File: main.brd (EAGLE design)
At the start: 45.1 x 39.4 mm, 12 parts, among them IC1 4001N, IC2 4069N, IC3 ISO1050DUB, IC4 ISO1050DUB, IC5 LD117AV33

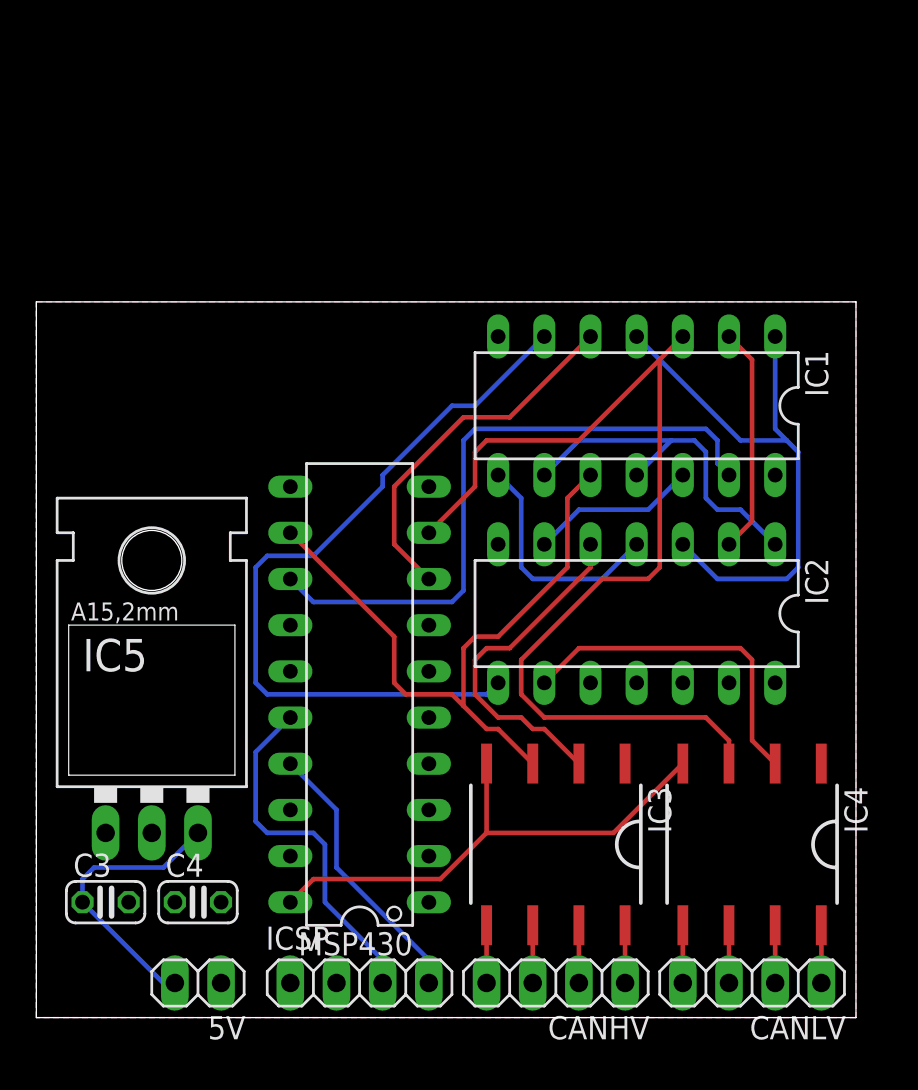
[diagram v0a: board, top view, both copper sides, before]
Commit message: Pin pitch of TI's MSP430 N20 package now aligns with grid
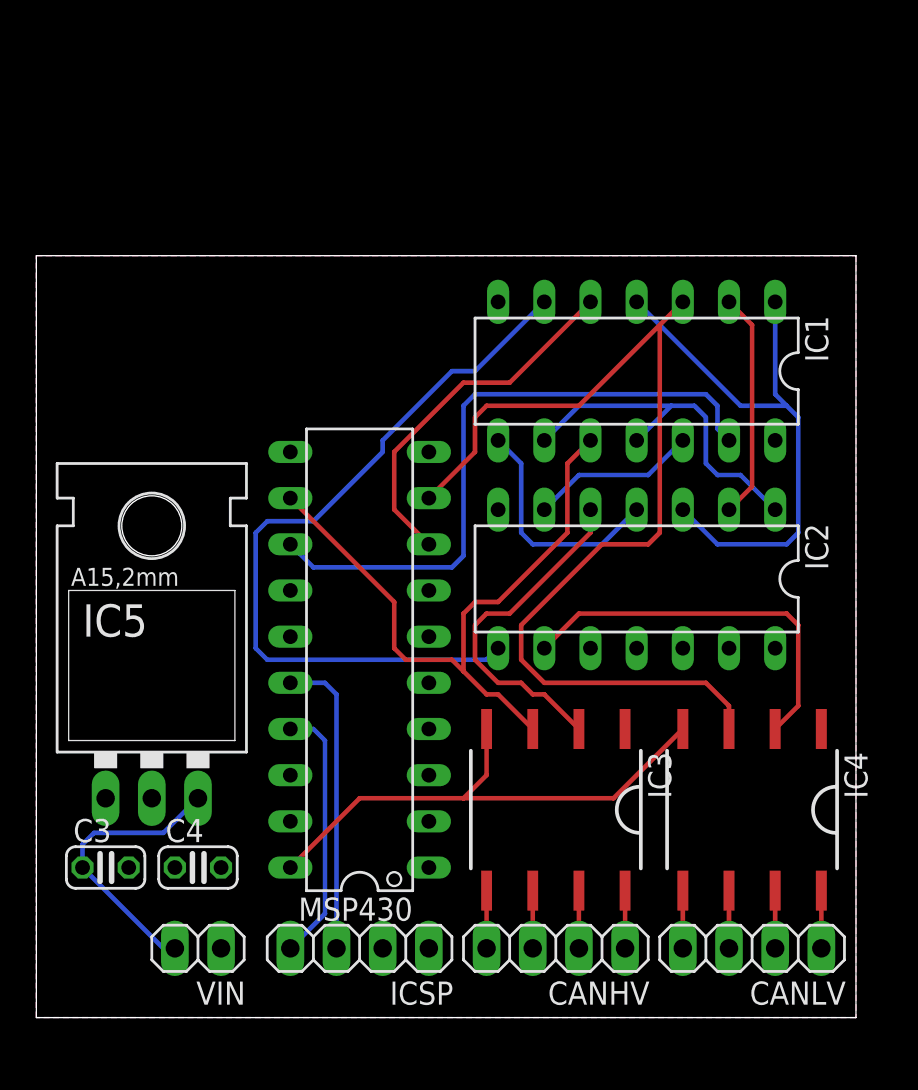
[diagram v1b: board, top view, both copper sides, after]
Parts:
- removed 5V: (no value), pinhead:1X02
- added VIN: (no value), pinhead:1X02
- moved C3 1.91 mm to (3.81, 8.26)
- moved C4 1.91 mm to (8.89, 8.26)
- moved IC1 1.91 mm to (33.0, 35.6)
- moved CANHV 1.91 mm to (28.6, 3.81)
- moved CANLV 1.91 mm to (39.4, 3.81)
- moved ICSP 1.91 mm to (17.8, 3.81), turned to 180 degrees
- moved IC3 1.90 mm to (28.6, 11.4)
- moved IC4 1.90 mm to (39.4, 11.4)
- moved IC5 1.90 mm to (6.35, 15.9)
- moved IC2 1.90 mm to (33.0, 24.1)
- moved MSP430 1.90 mm to (17.8, 19.7)
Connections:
- net GND: now also VIN.1; no longer 5V.1
- net N$23: now also VIN.2; no longer 5V.2
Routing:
- net N$1: track 19.8 -> 16.8 mm
- net N$20: track 18.7 -> 21.3 mm
- net GND: track 28.6 -> 30.4 mm
- net N$2: track 15.2 -> 14.4 mm
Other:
- board size 45.1 x 39.4 mm -> 45.1 x 41.9 mm

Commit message: Reduced board height a bit
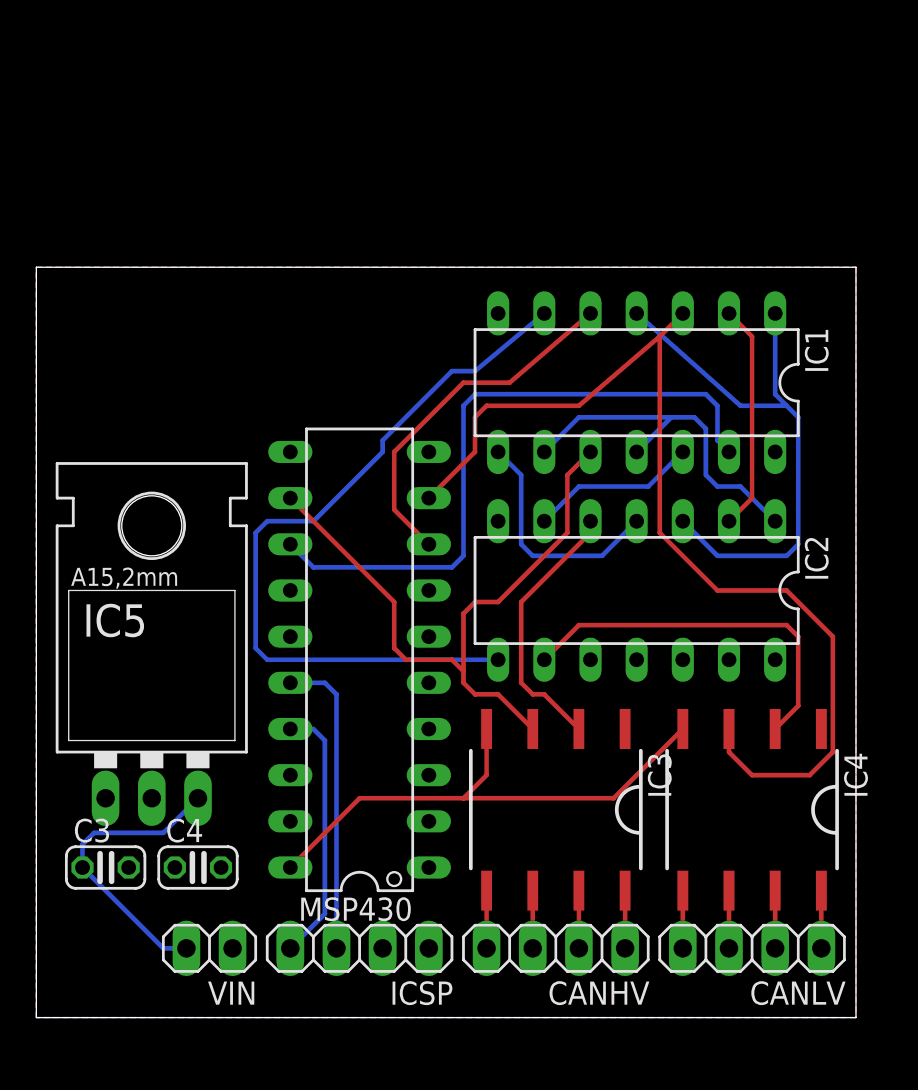
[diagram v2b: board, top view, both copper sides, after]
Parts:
- moved IC1 0.64 mm to (33.0, 34.9)
- moved VIN 0.63 mm to (9.53, 3.81)
- moved IC2 0.63 mm to (33.0, 23.5)
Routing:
- net N$18: track 18.9 -> 14.7 mm
- net N$3: track 41.7 -> 41.0 mm
- net N$22: track 35.2 -> 35.9 mm
- net N$23: track 15.6 -> 16.2 mm
- net N$20: track 21.3 -> 20.6 mm
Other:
- board size 45.1 x 41.9 mm -> 45.1 x 41.3 mm

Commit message: Replaced MSP430 with correct IC (MSP430G2553), improved board annotations, and added parts list to README
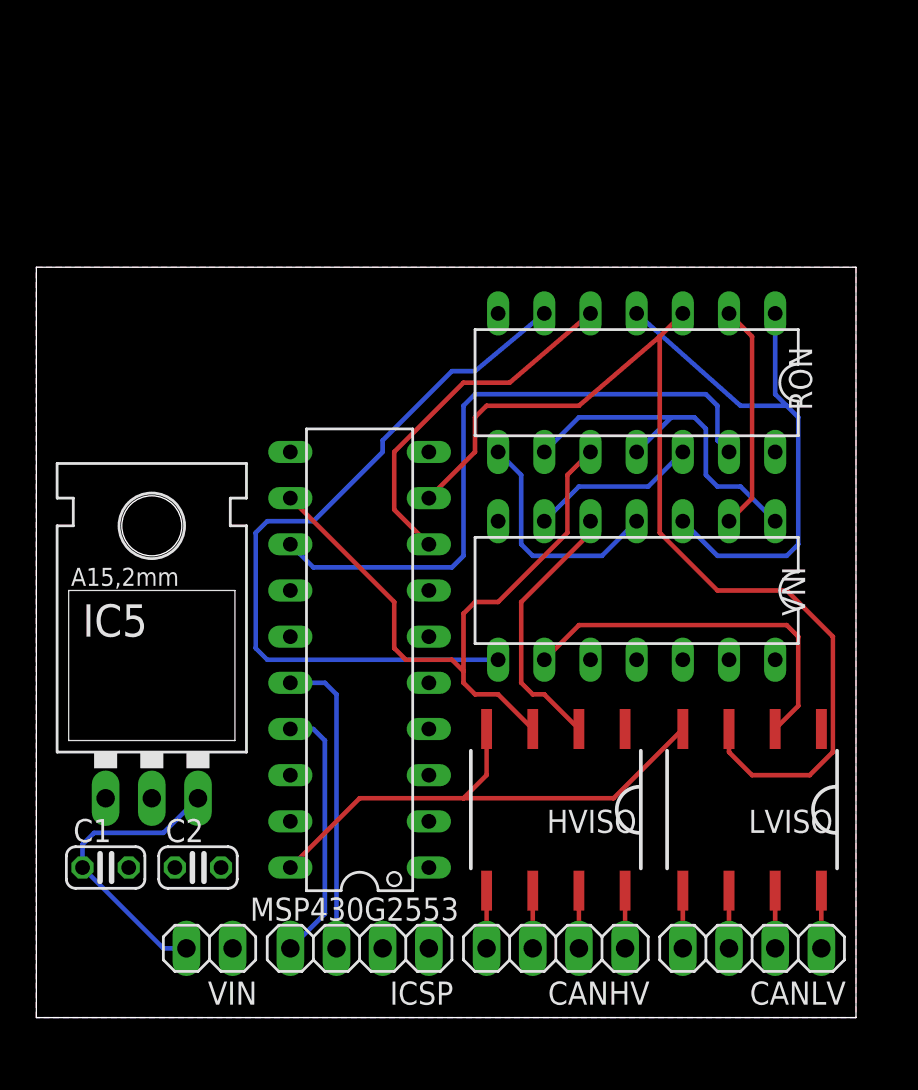
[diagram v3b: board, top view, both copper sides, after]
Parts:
- C1: value 100nf -> 0.1uF
- C2: value 10uf -> 10uF
- HVISO, LVISO: value ISO1050DUB -> (none)
- MSP430G2553: value G2X[0/3]2---N20 -> (none)
- renumbered C3 to C1, C4 to C2, IC1 to RON, IC2 to VNI, IC3 to HVISO, IC4 to LVISO, MSP430 to MSP430G2553

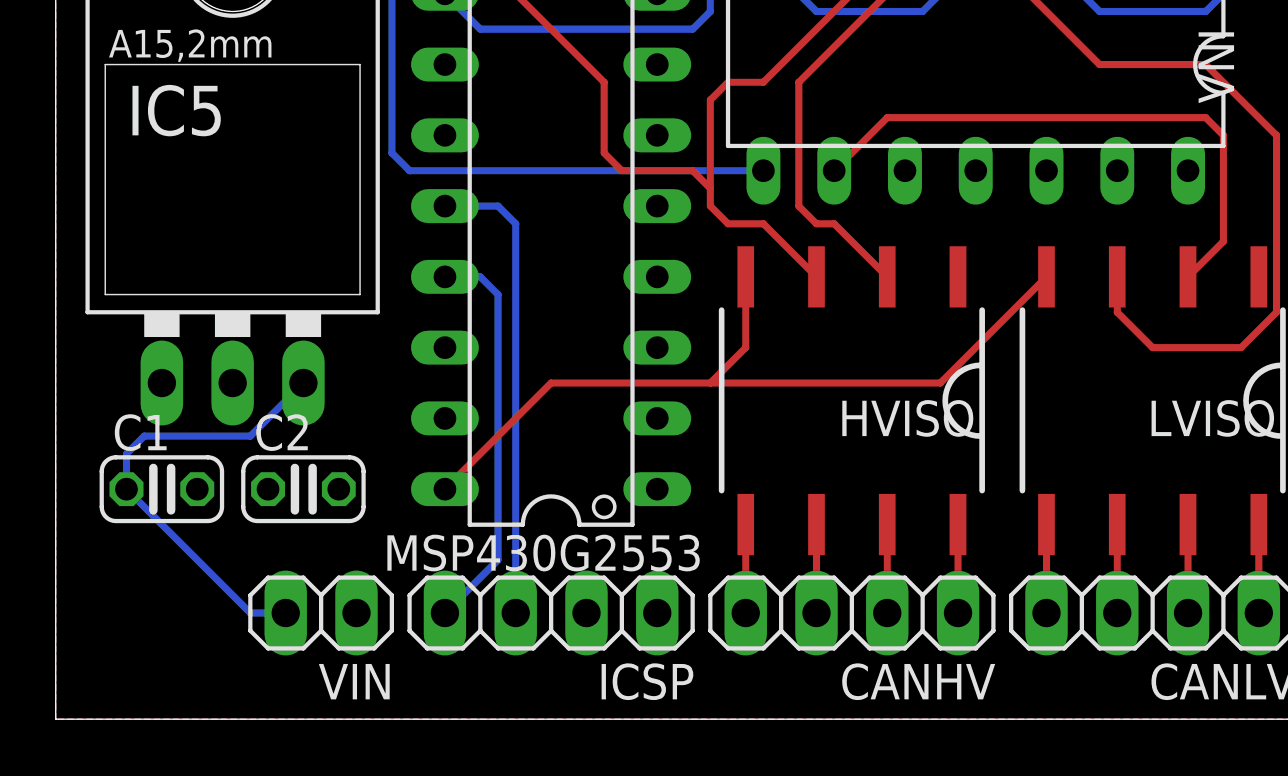
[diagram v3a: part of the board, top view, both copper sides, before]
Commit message: Moved some traces to the top layer
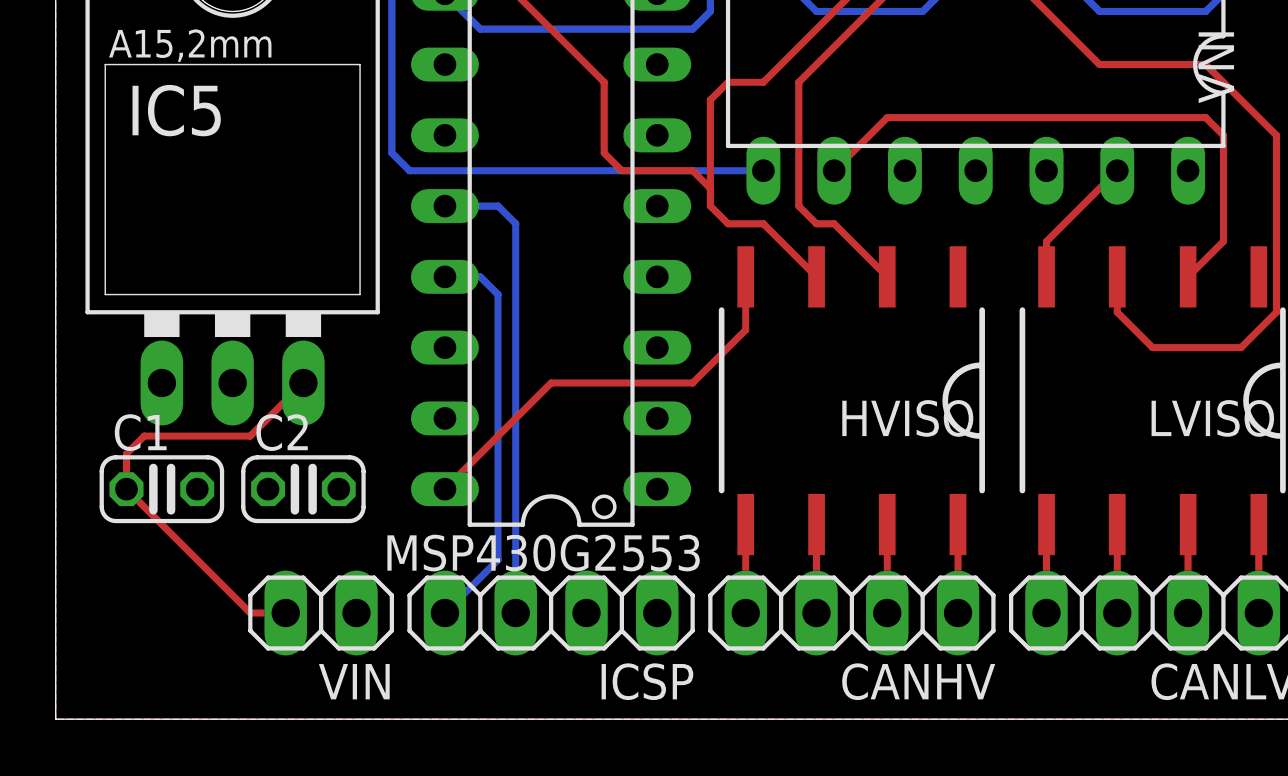
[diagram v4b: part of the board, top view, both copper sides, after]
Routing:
- net GND: track 30.4 -> 21.2 mm
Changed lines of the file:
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@@
 <vertex x="45.085" y="0"/>
 </polygon>
-<wire x1="17.78" y1="12.065" x2="23.495" y2="12.065" width="0.254" layer="1"/>
 <contactref element="VNI" pad="11"/>
 <contactref element="VNI" pad="13"/>
-<wire x1="23.495" y1="12.065" x2="31.75" y2="12.065" width="0.254" layer="1"/>
-<wire x1="24.765" y1="15.875" x2="24.765" y2="13.335" width="0.254" layer="1"/>
-<wire x1="31.75" y1="12.065" x2="35.56" y2="15.875" width="0.254" layer="1"/>
-<wire x1="24.765" y1="13.335" x2="23.495" y2="12.065" width="0.254" layer="1"/>
 <wire x1="24.765" y1="15.875" x2="24.765" y2="16.51" width="0.254" layer="1"/>
 <wire x1="35.56" y1="15.875" x2="35.56" y2="16.51" width="0.254" layer="1"/>
 <contactref element="MSP430G2553" pad="20"/>
-<wire x1="17.78" y1="12.065" x2="13.97" y2="8.255" width="0.254" layer="1"/>
+<wire x1="35.56" y1="15.875" x2="35.56" y2="17.145" width="0.254" layer="1"/>
+<wire x1="35.56" y1="17.145" x2="38.1" y2="19.685" width="0.254" layer="1"/>
+<wire x1="13.97" y1="8.255" x2="17.78" y2="12.065" width="0.254" layer="1"/>
+<wire x1="17.78" y1="12.065" x2="22.86" y2="12.065" width="0.254" layer="1"/>
+<wire x1="22.86" y1="12.065" x2="24.765" y2="13.97" width="0.254" layer="1"/>
+<wire x1="24.765" y1="13.97" x2="24.765" y2="15.875" width="0.254" layer="1"/>
 </signal>
 <signal name="N$1">
@@
 <contactref element="C1" pad="1"/>
 <contactref element="VIN" pad="2"/>
-<wire x1="8.255" y1="3.81" x2="6.985" y2="3.81" width="0.254" layer="16"/>
-<wire x1="6.985" y1="3.81" x2="2.54" y2="8.255" width="0.254" layer="16"/>
-<wire x1="2.54" y1="8.255" x2="2.54" y2="9.525" width="0.254" layer="16"/>
-<wire x1="2.54" y1="9.525" x2="3.175" y2="10.16" width="0.254" layer="16"/>
-<wire x1="3.175" y1="10.16" x2="6.985" y2="10.16" width="0.254" layer="16"/>
-<wire x1="6.985" y1="10.16" x2="8.89" y2="12.065" width="0.254" layer="16"/>
+<wire x1="8.255" y1="3.81" x2="6.985" y2="3.81" width="0.254" layer="1"/>
+<wire x1="6.985" y1="3.81" x2="2.54" y2="8.255" width="0.254" layer="1"/>
+<wire x1="2.54" y1="8.255" x2="2.54" y2="9.525" width="0.254" layer="1"/>
+<wire x1="2.54" y1="9.525" x2="3.175" y2="10.16" width="0.254" layer="1"/>
+<wire x1="3.175" y1="10.16" x2="6.985" y2="10.16" width="0.254" layer="1"/>
+<wire x1="6.985" y1="10.16" x2="8.89" y2="12.065" width="0.254" layer="1"/>
 </signal>
 <signal name="N$9">

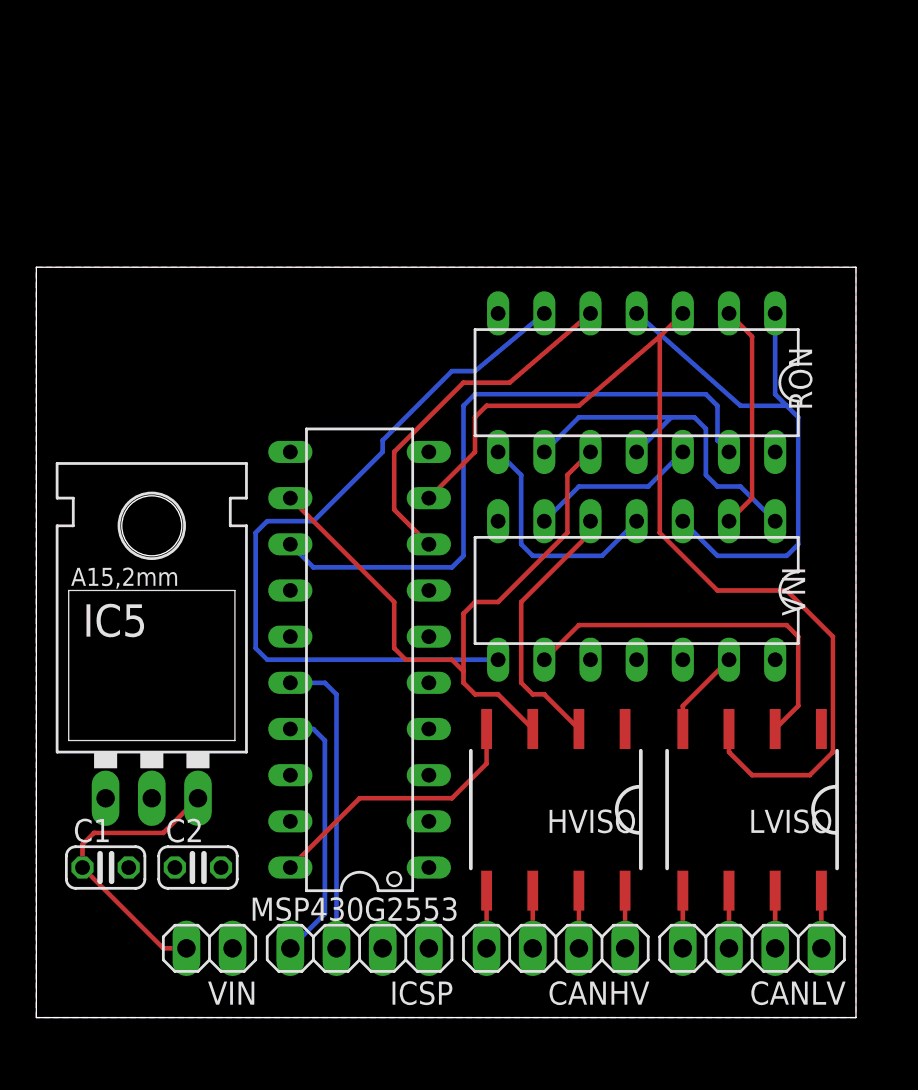
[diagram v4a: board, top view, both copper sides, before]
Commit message: PCB tweaks in pursuit of a planar design (not working)
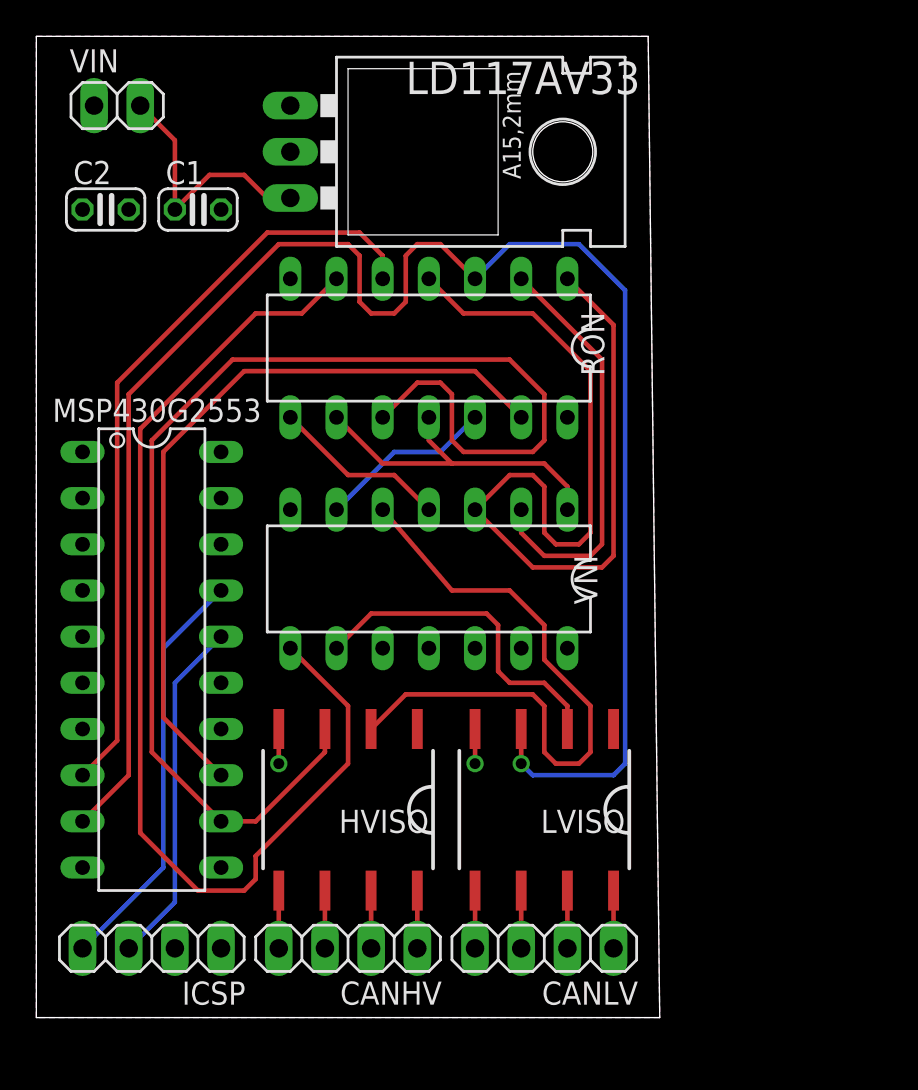
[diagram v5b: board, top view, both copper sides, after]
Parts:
- removed IC5: LD117AV33, v-reg:TO220L1
- added LD117AV33: (no value), v-reg:TO220L1
- moved VIN 46.6 mm to (4.45, 50.2), turned to 0 degrees
- moved C1 36.5 mm to (8.89, 44.5)
- moved C2 36.5 mm to (3.81, 44.5)
- moved RON 11.6 mm to (21.6, 36.8)
- moved VNI 11.4 mm to (21.6, 24.1)
- moved ICSP 11.4 mm to (6.35, 3.81)
- moved MSP430G2553 11.4 mm to (6.35, 19.7), turned to 270 degrees
- moved CANHV 11.4 mm to (17.1, 3.81)
- moved HVISO 11.4 mm to (17.1, 11.4)
- moved CANLV 11.4 mm to (27.9, 3.81)
- moved LVISO 11.4 mm to (27.9, 11.4)
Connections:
- net GND: now also LD117AV33.1; no longer IC5.1
- net N$23: now also LD117AV33.3; no longer IC5.3
- net VCC: now also LD117AV33.2; no longer IC5.2
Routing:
- net N$24: track 56.2 -> 98.2 mm, vias 0 -> 1
- net N$25: track 36.2 -> 70.9 mm
- net N$8: track 30.8 -> 55.8 mm
- net N$21: track 19.7 -> 42.2 mm
- net N$18: track 14.7 -> 35.9 mm
- net N$3: track 41.0 -> 60.5 mm
- net GND: track 21.2 -> 5.08 mm, vias 0 -> 2
- net N$4: track 12.5 -> 23.0 mm
- net N$2: track 14.4 -> 22.8 mm
- net N$22: track 35.9 -> 41.7 mm
- net N$5: track 13.0 -> 9.72 mm
- net N$1: track 16.8 -> 19.2 mm
- net N$20: track 20.6 -> 18.4 mm
- net N$23: track 16.2 -> 14.2 mm
- net N$7: track 20.0 -> 18.6 mm
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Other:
- board size 45.1 x 41.3 mm -> 34.3 x 54 mm

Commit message: Moved some traces to the bottom layer to fix plane isolation and shorten the trace lengths
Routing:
- net N$8: track 55.8 -> 34.7 mm
- net N$24: track 98.2 -> 88.4 mm, vias 1 -> 0
- net N$21: track 42.2 -> 36.4 mm
- net GND: track 5.08 -> 3.81 mm
